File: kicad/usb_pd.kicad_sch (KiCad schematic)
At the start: 15 parts, among them J13 USB-C, U10 STUSB4500, U9 USBLC6-2SC6

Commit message: Pick JLCPCB parts for the whole BOM and add BOM/CPL generation
Adds bom/parts.csv (LCSC numbers and MPNs), scripts to apply it to the schematic and
board and to generate the JLCPCB BOM, CPL and a live stock report. Swaps the
BOOTSEL/RESET switch to a basic 5.1 mm part with a matching footprint, and replaces
out-of-stock parts (SS54, WS2812B, 10u caps, SWD header).

Co-Authored-By: Claude Sonnet 5.5 <noreply@anthropic.com>
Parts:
- C46: LCSC (none) -> C1779; MPN (none) -> CL21A475KAQNNNE
- C47, C48: LCSC (none) -> C52923; MPN (none) -> CL05A105KA5NQNC
- C49: LCSC (none) -> C5673; MPN (none) -> CL10A105KA8NNNC
- R38, R39: LCSC (none) -> C11702; MPN (none) -> 0402WGF1001TCE
- R40: LCSC (none) -> C25744; MPN (none) -> 0402WGF1002TCE
- R41, R42: LCSC (none) -> C25741; MPN (none) -> 0402WGF1003TCE
- R43: LCSC (none) -> C25900; MPN (none) -> 0402WGF4701TCE
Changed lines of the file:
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@@
     (stroke (width 0) (type default))
   )
-  (wire (pts (xy 254.0 167.64) (xy 254.0 162.56))
+  (wire (pts (xy 254 167.64) (xy 254 162.56))
     (stroke (width 0) (type default))
   )
@@
     (stroke (width 0) (type default))
   )
-  (wire (pts (xy 254.0 213.36) (xy 254.0 218.44))
-    (stroke (width 0) (type default))
-  )
-  (wire (pts (xy 254.0 213.36) (xy 254.0 218.44))
+  (wire (pts (xy 254 213.36) (xy 254 218.44))
+    (stroke (width 0) (type default))
+  )
+  (wire (pts (xy 254 213.36) (xy 254 218.44))
     (stroke (width 0) (type default))
   )
@@
       (effects (font (size 1.27 1.27)) hide)
     )
+    (property "LCSC" "C1779" (id 4) (at 64.135 187.96 0)
+      (effects (font (size 1.27 1.27)) hide)
+    )
+    (property "MPN" "CL21A475KAQNNNE" (id 5) (at 64.135 187.96 0)
+      (effects (font (size 1.27 1.27)) hide)
+    )
     (pin "1")
     (pin "2")
@@
     )
   )
-  (symbol (lib_id "Interface_USB:STUSB4500QTR") (at 254.0 190.5 0) (unit 1)
+  (symbol (lib_id "Interface_USB:STUSB4500QTR") (at 254 190.5 0) (unit 1)
     (in_bom yes) (on_board yes) (dnp no)
     (property "Reference" "U10" (id 0) (at 241.3 168.91 0)
@@
       (effects (font (size 1.27 1.27)))
     )
-    (property "Footprint" "Package_DFN_QFN:QFN-24-1EP_4x4mm_P0.5mm_EP2.7x2.7mm" (id 2) (at 254.0 190.5 0)
-      (effects (font (size 1.27 1.27)) hide)
-    )
-    (property "Datasheet" "" (id 3) (at 254.0 190.5 0)
-      (effects (font (size 1.27 1.27)) hide)
-    )
-    (property "MPN" "STUSB4500QTR" (id 4) (at 254.0 190.5 0)
-      (effects (font (size 1.27 1.27)) hide)
-    )
-    (property "LCSC" "C2678061" (id 5) (at 254.0 190.5 0)
+    (property "Footprint" "Package_DFN_QFN:QFN-24-1EP_4x4mm_P0.5mm_EP2.7x2.7mm" (id 2) (at 254 190.5 0)
+      (effects (font (size 1.27 1.27)) hide)
+    )
+    (property "Datasheet" "" (id 3) (at 254 190.5 0)
+      (effects (font (size 1.27 1.27)) hide)
+    )
+    (property "MPN" "STUSB4500QTR" (id 4) (at 254 190.5 0)
+      (effects (font (size 1.27 1.27)) hide)
+    )
+    (property "LCSC" "C2678061" (id 5) (at 254 190.5 0)
       (effects (font (size 1.27 1.27)) hide)
     )
@@
     )
   )
-  (symbol (lib_id "power:+3.3VA") (at 254.0 162.56 0) (unit 1)
-    (in_bom no) (on_board no) (dnp no)
-    (property "Reference" "#PWR7009" (id 0) (at 254.0 166.37 0)
-      (effects (font (size 1.27 1.27)) hide)
-    )
-    (property "Value" "+3V3_AUX" (id 1) (at 254.0 159.004 0)
-      (effects (font (size 1.27 1.27)))
-    )
-    (property "Footprint" "" (id 2) (at 254.0 162.56 0)
-      (effects (font (size 1.27 1.27)) hide)
-    )
-    (property "Datasheet" "" (id 3) (at 254.0 162.56 0)
+  (symbol (lib_id "power:+3.3VA") (at 254 162.56 0) (unit 1)
+    (in_bom no) (on_board no) (dnp no)
+    (property "Reference" "#PWR7009" (id 0) (at 254 166.37 0)
+      (effects (font (size 1.27 1.27)) hide)
+    )
+    (property "Value" "+3V3_AUX" (id 1) (at 254 159.004 0)
+      (effects (font (size 1.27 1.27)))
+    )
+    (property "Footprint" "" (id 2) (at 254 162.56 0)
+      (effects (font (size 1.27 1.27)) hide)
+    )
+    (property "Datasheet" "" (id 3) (at 254 162.56 0)
       (effects (font (size 1.27 1.27)) hide)
     )
@@
     )
   )
-  (symbol (lib_id "power:GND") (at 254.0 218.44 0) (unit 1)
-    (in_bom no) (on_board no) (dnp no)
-    (property "Reference" "#PWR7010" (id 0) (at 254.0 224.79 0)
-      (effects (font (size 1.27 1.27)) hide)
-    )
-    (property "Value" "GND" (id 1) (at 254.0 222.25 0)
-      (effects (font (size 1.27 1.27)))
-    )
-    (property "Footprint" "" (id 2) (at 254.0 218.44 0)
-      (effects (font (size 1.27 1.27)) hide)
-    )
-    (property "Datasheet" "" (id 3) (at 254.0 218.44 0)
+  (symbol (lib_id "power:GND") (at 254 218.44 0) (unit 1)
+    (in_bom no) (on_board no) (dnp no)
+    (property "Reference" "#PWR7010" (id 0) (at 254 224.79 0)
+      (effects (font (size 1.27 1.27)) hide)
+    )
+    (property "Value" "GND" (id 1) (at 254 222.25 0)
+      (effects (font (size 1.27 1.27)))
+    )
+    (property "Footprint" "" (id 2) (at 254 218.44 0)
+      (effects (font (size 1.27 1.27)) hide)
+    )
+    (property "Datasheet" "" (id 3) (at 254 218.44 0)
       (effects (font (size 1.27 1.27)) hide)
     )
@@
     )
   )
-  (symbol (lib_id "power:GND") (at 254.0 218.44 0) (unit 1)
-    (in_bom no) (on_board no) (dnp no)
-    (property "Reference" "#PWR7011" (id 0) (at 254.0 224.79 0)
-      (effects (font (size 1.27 1.27)) hide)
-    )
-    (property "Value" "GND" (id 1) (at 254.0 222.25 0)
-      (effects (font (size 1.27 1.27)))
-    )
-    (property "Footprint" "" (id 2) (at 254.0 218.44 0)
-      (effects (font (size 1.27 1.27)) hide)
-    )
-    (property "Datasheet" "" (id 3) (at 254.0 218.44 0)
+  (symbol (lib_id "power:GND") (at 254 218.44 0) (unit 1)
+    (in_bom no) (on_board no) (dnp no)
+    (property "Reference" "#PWR7011" (id 0) (at 254 224.79 0)
+      (effects (font (size 1.27 1.27)) hide)
+    )
+    (property "Value" "GND" (id 1) (at 254 222.25 0)
+      (effects (font (size 1.27 1.27)))
+    )
+    (property "Footprint" "" (id 2) (at 254 218.44 0)
+      (effects (font (size 1.27 1.27)) hide)
+    )
+    (property "Datasheet" "" (id 3) (at 254 218.44 0)
       (effects (font (size 1.27 1.27)) hide)
     )
@@
       (effects (font (size 1.27 1.27)) hide)
     )
+    (property "LCSC" "C52923" (id 4) (at 330.835 111.76 0)
+      (effects (font (size 1.27 1.27)) hide)
+    )
+    (property "MPN" "CL05A105KA5NQNC" (id 5) (at 330.835 111.76 0)
+      (effects (font (size 1.27 1.27)) hide)
+    )
     (pin "1")
     (pin "2")
@@
       (effects (font (size 1.27 1.27)) hide)
     )
+    (property "LCSC" "C52923" (id 4) (at 346.075 111.76 0)
+      (effects (font (size 1.27 1.27)) hide)
+    )
+    (property "MPN" "CL05A105KA5NQNC" (id 5) (at 346.075 111.76 0)
+      (effects (font (size 1.27 1.27)) hide)
+    )
     (pin "1")
     (pin "2")
@@
       (effects (font (size 1.27 1.27)) hide)
     )
+    (property "LCSC" "C5673" (id 4) (at 361.315 111.76 0)
+      (effects (font (size 1.27 1.27)) hide)
+    )
+    (property "MPN" "CL10A105KA8NNNC" (id 5) (at 361.315 111.76 0)
+      (effects (font (size 1.27 1.27)) hide)
+    )
     (pin "1")
     (pin "2")
@@
       (effects (font (size 1.27 1.27)) hide)
     )
+    (property "LCSC" "C11702" (id 4) (at 332.232 152.4 0)
+      (effects (font (size 1.27 1.27)) hide)
+    )
+    (property "MPN" "0402WGF1001TCE" (id 5) (at 332.232 152.4 0)
+      (effects (font (size 1.27 1.27)) hide)
+    )
     (pin "1")
     (pin "2")
@@
       (effects (font (size 1.27 1.27)) hide)
     )
+    (property "LCSC" "C11702" (id 4) (at 347.472 152.4 0)
+      (effects (font (size 1.27 1.27)) hide)
+    )
+    (property "MPN" "0402WGF1001TCE" (id 5) (at 347.472 152.4 0)
+      (effects (font (size 1.27 1.27)) hide)
+    )
     (pin "1")
     (pin "2")
@@
       (effects (font (size 1.27 1.27)) hide)
     )
+    (property "LCSC" "C25744" (id 4) (at 362.712 152.4 0)
+      (effects (font (size 1.27 1.27)) hide)
+    )
+    (property "MPN" "0402WGF1002TCE" (id 5) (at 362.712 152.4 0)
+      (effects (font (size 1.27 1.27)) hide)
+    )
     (pin "1")
     (pin "2")
@@
       (effects (font (size 1.27 1.27)) hide)
     )
+    (property "LCSC" "C25741" (id 4) (at 377.952 152.4 0)
+      (effects (font (size 1.27 1.27)) hide)
+    )
+    (property "MPN" "0402WGF1003TCE" (id 5) (at 377.952 152.4 0)
+      (effects (font (size 1.27 1.27)) hide)
+    )
     (pin "1")
     (pin "2")
@@
       (effects (font (size 1.27 1.27)) hide)
     )
+    (property "LCSC" "C25741" (id 4) (at 393.192 152.4 0)
+      (effects (font (size 1.27 1.27)) hide)
+    )
+    (property "MPN" "0402WGF1003TCE" (id 5) (at 393.192 152.4 0)
+      (effects (font (size 1.27 1.27)) hide)
+    )
     (pin "1")
     (pin "2")
@@
       (effects (font (size 1.27 1.27)) hide)
     )
+    (property "LCSC" "C25900" (id 4) (at 408.432 152.4 0)
+      (effects (font (size 1.27 1.27)) hide)
+    )
+    (property "MPN" "0402WGF4701TCE" (id 5) (at 408.432 152.4 0)
+      (effects (font (size 1.27 1.27)) hide)
+    )

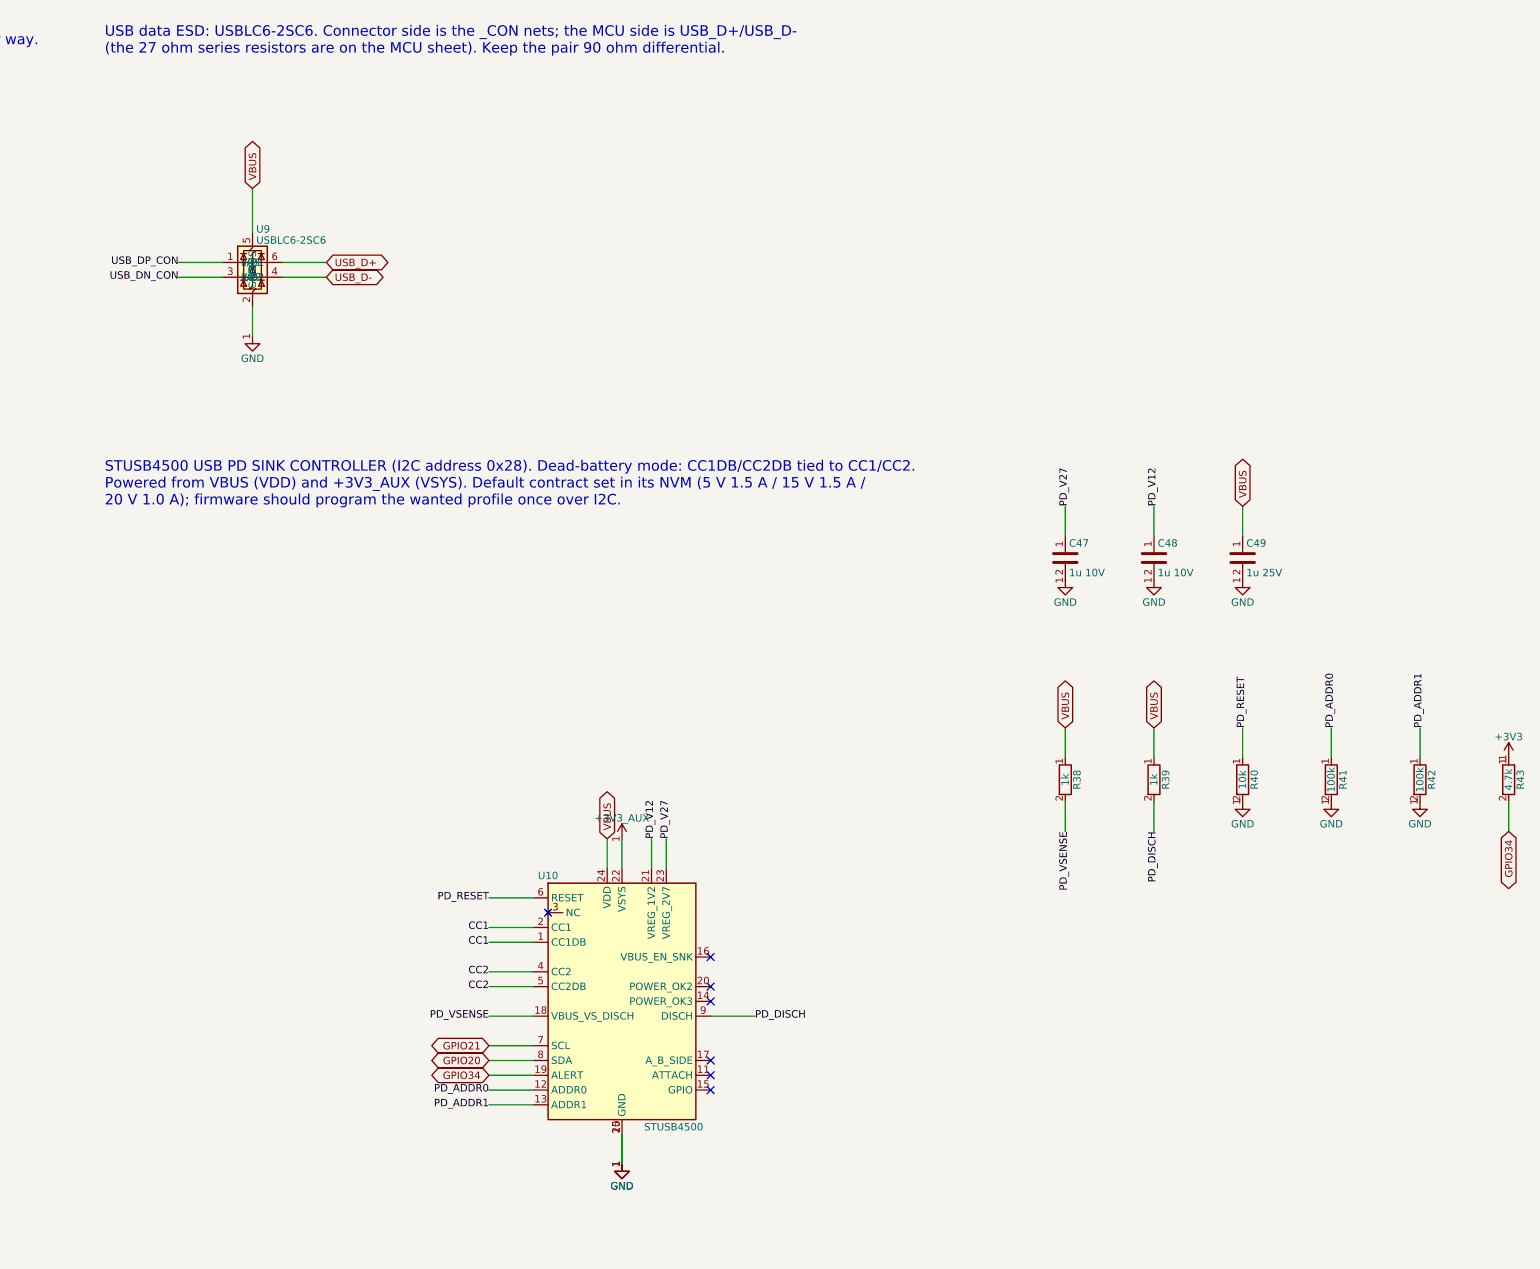
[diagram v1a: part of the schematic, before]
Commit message: Rework board layout, swap SWD header to through-hole, add Qwiic port
- SWD (J10) is now a 1x3 2.54 mm through-hole pin header footprint
  (SWCLK, GND, SWDIO) instead of the JST SH connector; removed from the
  JLCPCB BOM.
- Add J20 Qwiic connector (XY-SM04B-SRSS-TB) on the I2C bus: GND, +3V3,
  GPIO20 (SDA), GPIO21 (SCL), mounting tabs to GND.
- Placement/routing progress and the helper scripts used for it.

DRC still reports open items (unrouted RUN/GPIO24/GPIO29/QSPI_SD0 nets,
R108/GPIO23 and NT1/GPIO20 shorts, J12 edge clearance, silkscreen
overlaps); to be fixed in follow-up commits.

Co-Authored-By: Claude Sonnet 5.5 <noreply@anthropic.com>
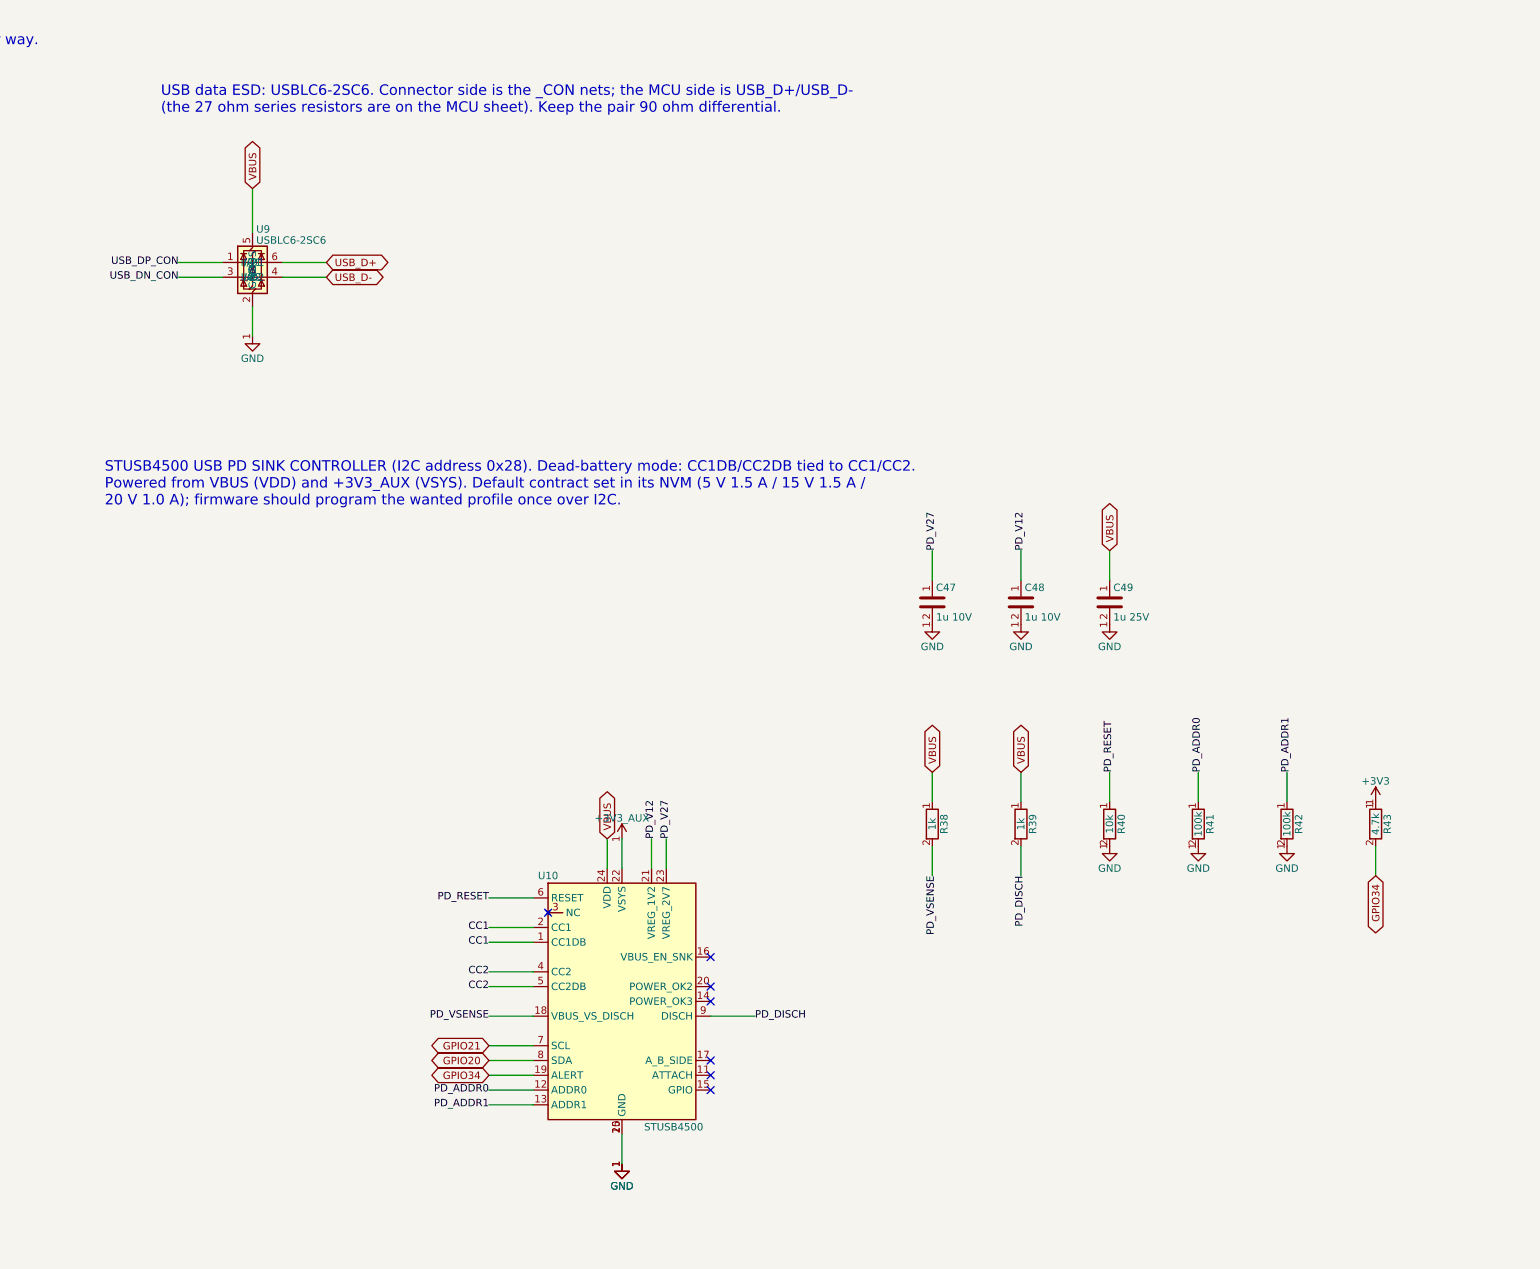
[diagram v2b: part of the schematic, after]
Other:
- moved on the sheet: C47, C48, C49, R38, R39, R40, R41, R42, R43
